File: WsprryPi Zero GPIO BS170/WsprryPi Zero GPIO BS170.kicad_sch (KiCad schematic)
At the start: 28 parts, among them J11 Socket_2x20_P2.54mm, J12 Conn_01x03, J41 SMA_Adafruit_1865, J42 J81/J82 LPF sockets, SW11 SKRPANE010, T21 WBC2-1TLC, T41 WBC2-1TLC, U11 Raspberry Pi 40-pin HAT inter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, U31 LTC6432AIUF-15#PBF, U51 TPS22918DBVR

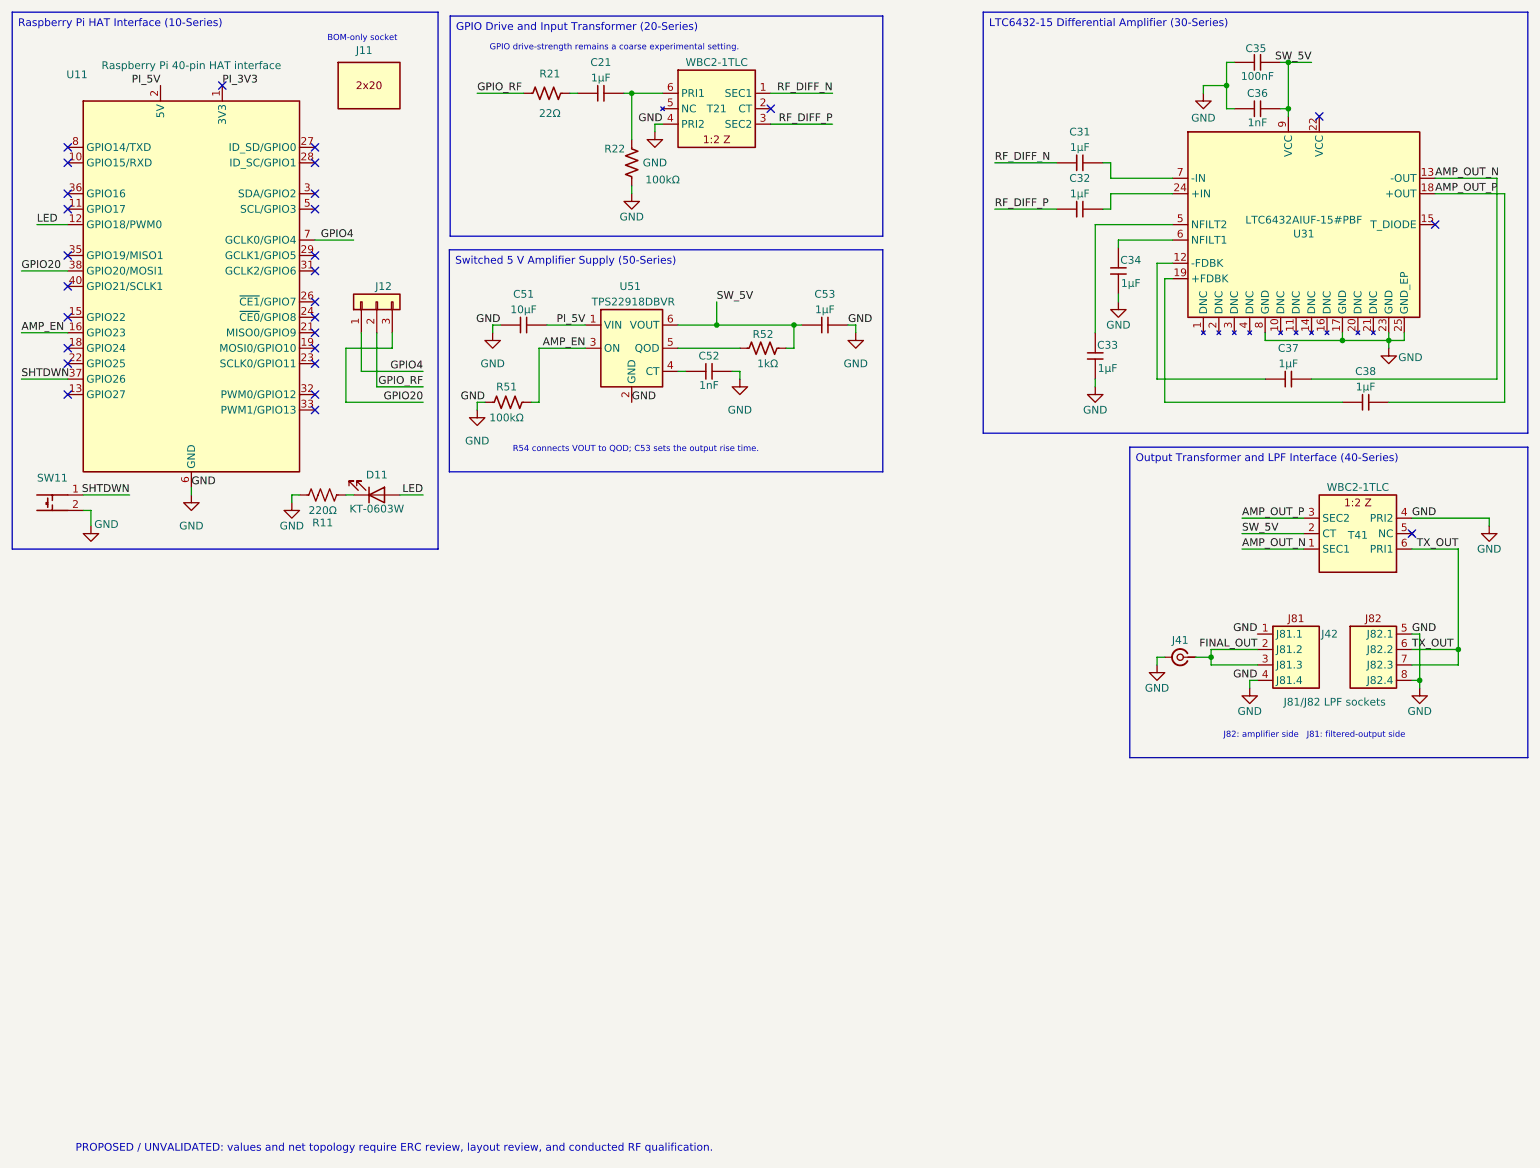
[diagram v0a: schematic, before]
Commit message: Universal GPIO wBS170
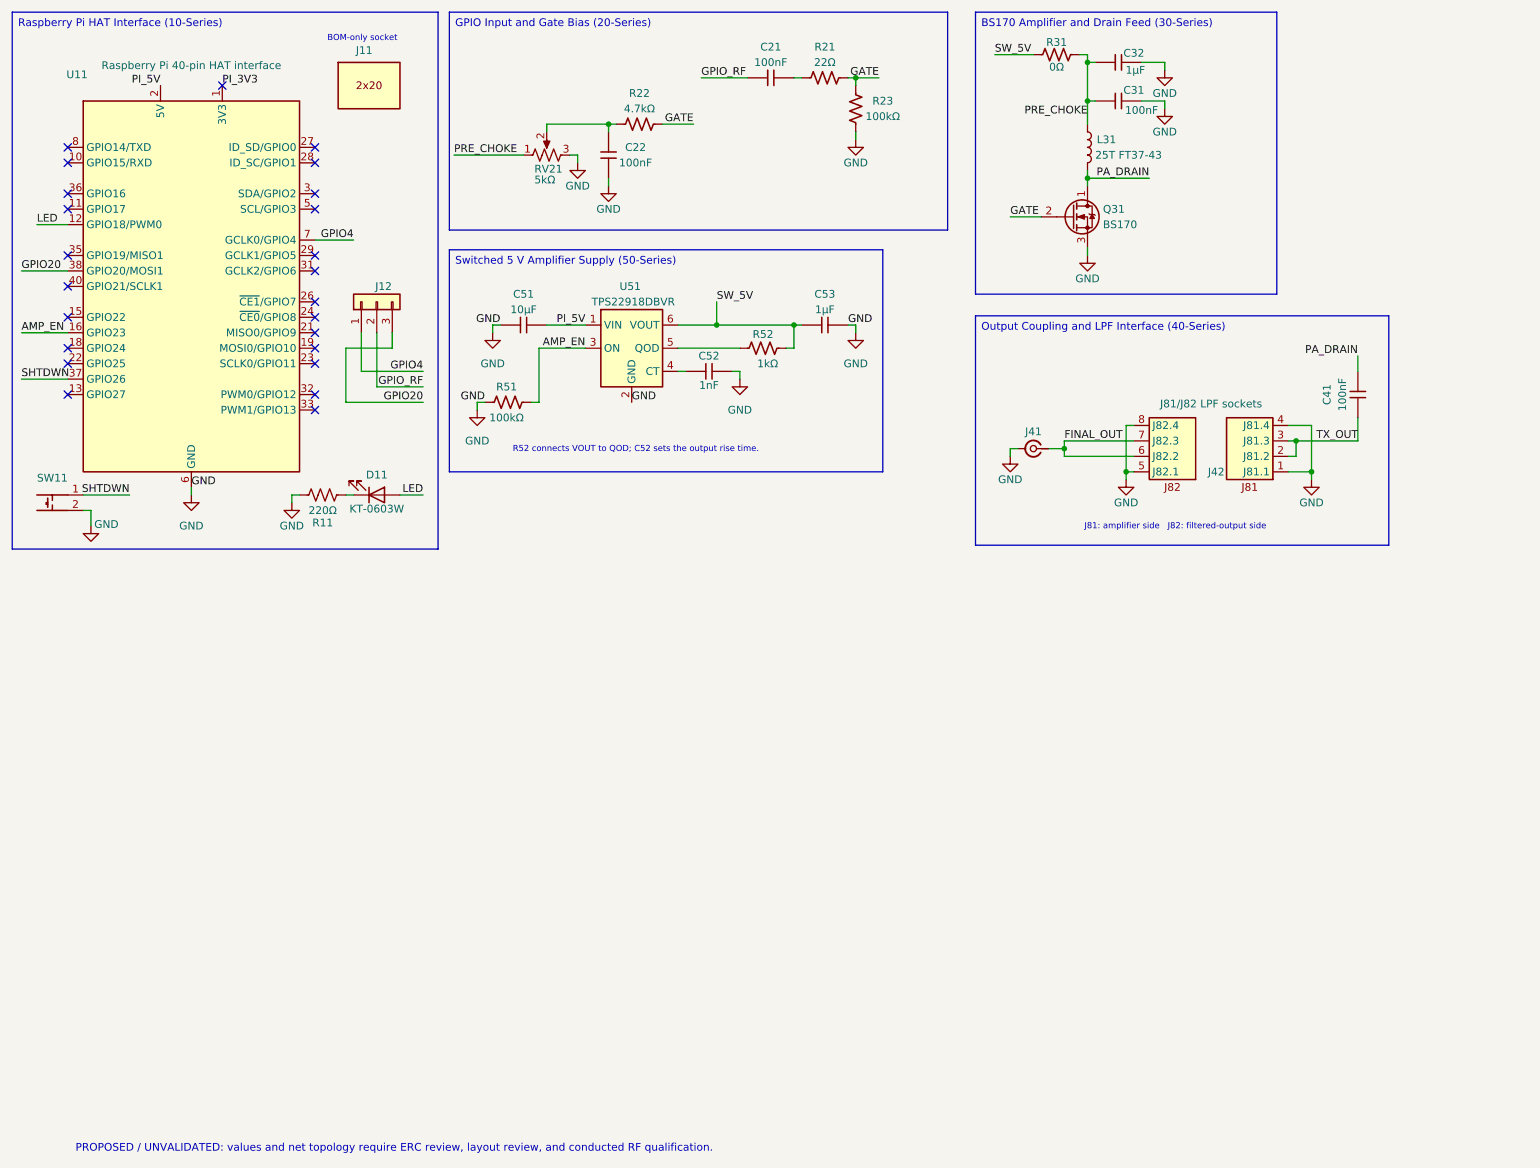
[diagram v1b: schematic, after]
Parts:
- removed C21, C31, C37, C38: 1µF, wsprrypi-zero-gpio-bs170:C_1206_3216Metric, symbol wsprrypi-zero-gpio-bs170:C_0805
- removed C33, C34: 1µF, wsprrypi-zero-gpio-bs170:C_0805_2012Metric, symbol wsprrypi-zero-gpio-bs170:C_0805
- removed C35: 100nF, wsprrypi-zero-gpio-bs170:C_0603_1608Metric, symbol wsprrypi-zero-gpio-bs170:C_0603
- removed C36: 1nF, wsprrypi-zero-gpio-bs170:C_0603_1608Metric, symbol wsprrypi-zero-gpio-bs170:C_0603
- removed T21, T41: WBC2-1TLC, wsprrypi-zero-gpio-bs170:Coilcraft_WBC2-1TLC, symbol wsprrypi-zero-gpio-bs170:WBC2-1TLC
- removed U31: LTC6432AIUF-15#PBF, wsprrypi-zero-gpio-bs170:Analog_UF24_QFN-24-1EP_4x4mm_P0.5mm_EP2.45x2.45mm_ThermalVias, symbol wsprrypi-zero-gpio-bs170:LTC6432-15
- added C21, C22, C31, C41: 100nF, wsprrypi-zero-gpio-bs170:C_0603_1608Metric, symbol wsprrypi-zero-gpio-bs170:C_0603
- added L31: 25T FT37-43, wsprrypi-zero-gpio-bs170:L_Toroid_FT37-43_Vertical_P5.08mm, symbol wsprrypi-zero-gpio-bs170:L
- added Q31: BS170, wsprrypi-zero-gpio-bs170:TO-92_Inline, symbol wsprrypi-zero-gpio-bs170:BS170
- added R23: 100kΩ, wsprrypi-zero-gpio-bs170:R_0603_1608Metric, symbol wsprrypi-zero-gpio-bs170:R_0603
- added R31: 0Ω, wsprrypi-zero-gpio-bs170:R_0805_2012Metric, symbol wsprrypi-zero-gpio-bs170:R_0805
- added RV21: 5kΩ, wsprrypi-zero-gpio-bs170:Potentiometer_Bourns_TC33X_Vertical, symbol wsprrypi-zero-gpio-bs170:R_Potentiometer_US
- C32: footprint wsprrypi-zero-gpio-bs170:C_1206_3216Metric -> wsprrypi-zero-gpio-bs170:C_0805_2012Metric; LCSC_PART C342628 -> (none)
- J42: now left out of the parts list
- R21: LCSC_PART C23186 -> (none)
- R22: value 100kΩ -> 4.7kΩ; LCSC_PART C14675 -> (none)
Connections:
- net RF_DIFF_P is gone; now on net GND: C32.1
- net FINAL_OUT: now also J42.6 (J82.2), J42.7 (J82.3); no longer J42.2 (J81.2), J42.3 (J81.3)
- net GND: now also C22.1, C31.1, Q31.3 (S), R23.1, RV21.3; no longer R22.1
- net GPIO_RF: now also C21.1; no longer R21.1
- net SW_5V: now also R31.1
- net TX_OUT: now also J42.2 (J81.2), J42.3 (J81.3), C41.1; no longer J42.6 (J82.2), J42.7 (J82.3)
- net PRE_CHOKE: now reaches C32.2
- net PRE_CHOKE: now also C31.2, L31.1, R31.2, RV21.1
- net GATE: now reaches R22.2
- net GATE: now also R21.2, Q31.2 (G), R23.2
- new net: C21.2, R21.1
- new net: C22.2, R22.1, RV21.2
- new net PA_DRAIN: C41.2, L31.2, Q31.1 (D)
- no-connect marks 28 -> 24
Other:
- note added: "J81: amplifier side J82: filtered-output side"
- note added: "R52 connects VOUT to QOD; C52 sets the output rise time."
- note removed: "GPIO drive-strength remains a coarse experimental setting."
- note removed: "J82: amplifier side J81: filtered-output side"
- note removed: "R54 connects VOUT to QOD; C53 sets the output rise time."
- title: WsprryPi Zero GPIO BS170 - Copied LTC6432 Baseline -> WsprryPi Zero GPIO BS170 - Unwired RF Stage
- moved on the sheet: J41, J42

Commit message: Renumber BS170 functional blocks and component references
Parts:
- renumbered C51 to C21, C52 to C22, C53 to C23, C21 to C31, C22 to C32, C31 to C41, C32 to C42, C41 to C51, J41 to J51, J42 to J52, L31 to L41, Q31 to Q41, R51 to R21, R52 to R22, R21 to R31, R22 to R32, R23 to R33, R31 to R41, RV21 to RV31, U51 to U21
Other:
- note added: "R22 connects VOUT to QOD; C22 sets the output rise time."
- note removed: "R52 connects VOUT to QOD; C52 sets the output rise time."
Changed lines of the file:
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@@
 		)
 	)
-	(text "R52 connects VOUT to QOD; C52 sets the output rise time."
+	(text "R22 connects VOUT to QOD; C22 sets the output rise time."
 		(exclude_from_sim no)
 		(at 97.282 87.122 0)
@@
 		)
 	)
-	(text_box "Output Coupling and LPF Interface (40-Series)"
+	(text_box "Output Coupling and LPF Interface (50-Series)"
 		(exclude_from_sim no)
 		(at 173.355 64.53 0)
@@
 		)
 	)
-	(text_box "GPIO Input and Gate Bias (20-Series)"
+	(text_box "GPIO Input and Gate Bias (30-Series)"
 		(exclude_from_sim no)
 		(at 86.86 14.605 0)
@@
 		)
 	)
-	(text_box "Switched 5 V Amplifier Supply (50-Series)"
+	(text_box "Switched 5 V Amplifier Supply (20-Series)"
 		(exclude_from_sim no)
 		(at 86.86 53.67 0)
@@
 		)
 	)
-	(text_box "BS170 Amplifier and Drain Feed (30-Series)"
+	(text_box "BS170 Amplifier and Drain Feed (40-Series)"
 		(exclude_from_sim no)
 		(at 173.355 14.605 0)
@@
 		(in_pos_files yes)
 		(dnp no)
-		(property "Reference" "C31"
+		(property "Reference" "C41"
 			(at 199.39 27.432 0)
 			(show_name no)
@@
 			(project "WsprryPi Zero GPIO BS170"
 				(path "/42fb2efa-c288-4686-a90a-043ad23a327d"
-					(reference "C31")
+					(reference "C41")
 					(unit 1)
 				)
@@
 		(in_pos_files yes)
 		(dnp no)
-		(property "Reference" "R21"
+		(property "Reference" "R31"
 			(at 148.59 20.32 0)
 			(show_name no)
@@
 			(project "WsprryPi Zero GPIO BS170"
 				(path "/42fb2efa-c288-4686-a90a-043ad23a327d"
-					(reference "R21")
+					(reference "R31")
 					(unit 1)
 				)
@@
 		(in_pos_files yes)
 		(dnp no)
-		(property "Reference" "C22"
+		(property "Reference" "C32"
 			(at 117.475 36.83 90)
 			(show_name no)
@@
 			(project "WsprryPi Zero GPIO BS170"
 				(path "/42fb2efa-c288-4686-a90a-043ad23a327d"
-					(reference "C22")
+					(reference "C32")
 					(unit 1)
 				)
@@
 		(in_pos_files yes)
 		(dnp no)
-		(property "Reference" "C21"
+		(property "Reference" "C31"
 			(at 139.7 20.32 0)
 			(show_name no)
@@
 			(project "WsprryPi Zero GPIO BS170"
 				(path "/42fb2efa-c288-4686-a90a-043ad23a327d"
-					(reference "C21")
+					(reference "C31")
 					(unit 1)
 				)
@@
 		(in_pos_files yes)
 		(dnp no)
-		(property "Reference" "J41"
+		(property "Reference" "J51"
 			(at 182.88 83.566 0)
 			(show_name no)
@@
 			(project "WsprryPi Zero GPIO BS170"
 				(path "/42fb2efa-c288-4686-a90a-043ad23a327d"
-					(reference "J41")
+					(reference "J51")
 					(unit 1)
 				)
@@
 		(in_pos_files no)
 		(dnp no)
-		(property "Reference" "L31"
+		(property "Reference" "L41"
 			(at 193.294 35.56 0)
 			(show_name no)
@@
 			(project "WsprryPi Zero GPIO BS170"
 				(path "/42fb2efa-c288-4686-a90a-043ad23a327d"
-					(reference "L31")
+					(reference "L41")
 					(unit 1)
 				)
@@
 		(in_pos_files yes)
 		(dnp no)
-		(property "Reference" "R23"
+		(property "Reference" "R33"
 			(at 158.115 29.21 90)
 			(show_name no)
@@
 			(project "WsprryPi Zero GPIO BS170"
 				(path "/42fb2efa-c288-4686-a90a-043ad23a327d"
-					(reference "R23")
+					(reference "R33")
 					(unit 1)
 				)
@@
 		(in_pos_files yes)
 		(dnp no)
-		(property "Reference" "C53"
+		(property "Reference" "C23"
 			(at 148.59 60.96 0)
 			(show_name no)
@@
 			(project "WsprryPi Zero GPIO BS170"
 				(path "/42fb2efa-c288-4686-a90a-043ad23a327d"
-					(reference "C53")
+					(reference "C23")
 					(unit 1)
 				)
@@
 		(in_pos_files yes)
 		(dnp no)
-		(property "Reference" "C32"
+		(property "Reference" "C42"
 			(at 199.39 21.336 0)
 			(show_name no)
@@
 			(project "WsprryPi Zero GPIO BS170"
 				(path "/42fb2efa-c288-4686-a90a-043ad23a327d"
-					(reference "C32")
+					(reference "C42")
 					(unit 1)
 				)
@@
 		(in_pos_files yes)
 		(dnp no)
-		(property "Reference" "C51"
+		(property "Reference" "C21"
 			(at 99.06 60.96 0)
 			(show_name no)
@@
 			(project "WsprryPi Zero GPIO BS170"
 				(path "/42fb2efa-c288-4686-a90a-043ad23a327d"
-					(reference "C51")
+					(reference "C21")
 					(unit 1)
 				)
@@
 		(in_pos_files yes)
 		(dnp no)
-		(property "Reference" "R22"
+		(property "Reference" "R32"
 			(at 118.11 27.94 0)
 			(show_name no)
@@
 			(project "WsprryPi Zero GPIO BS170"
 				(path "/42fb2efa-c288-4686-a90a-043ad23a327d"
-					(reference "R22")
+					(reference "R32")
 					(unit 1)
 				)
@@
 		(in_pos_files yes)
 		(dnp no)
-		(property "Reference" "Q31"
+		(property "Reference" "Q41"
 			(at 194.31 46.99 0)
 			(show_name no)
@@
 			(project "WsprryPi Zero GPIO BS170"
 				(path "/42fb2efa-c288-4686-a90a-043ad23a327d"
-					(reference "Q31")
+					(reference "Q41")
 					(unit 1)
 				)
@@
 		(in_pos_files no)
 		(dnp no)
-		(property "Reference" "J42"
+		(property "Reference" "J52"
 			(at 212.93 90.18 0)
 			(show_name no)
@@
 			(project "WsprryPi Zero GPIO BS170"
 				(path "/42fb2efa-c288-4686-a90a-043ad23a327d"
-					(reference "J42")
+					(reference "J52")
 					(unit 1)
 				)
@@
 		(in_pos_files yes)
 		(dnp no)
-		(property "Reference" "R31"
+		(property "Reference" "R41"
 			(at 186.69 19.558 0)
 			(show_name no)
@@
 			(project "WsprryPi Zero GPIO BS170"
 				(path "/42fb2efa-c288-4686-a90a-043ad23a327d"
-					(reference "R31")
+					(reference "R41")
 					(unit 1)
 				)
@@
 		(in_pos_files yes)
 		(dnp no)
-		(property "Reference" "C52"
+		(property "Reference" "C22"
 			(at 129.54 71.12 0)
 			(show_name no)
@@
 			(project "WsprryPi Zero GPIO BS170"
 				(path "/42fb2efa-c288-4686-a90a-043ad23a327d"
-					(reference "C52")
+					(reference "C22")
 					(unit 1)
 				)
@@
 		(in_pos_files yes)
 		(dnp no)
-		(property "Reference" "U51"
+		(property "Reference" "U21"
 			(at 116.586 59.69 0)
 			(show_name no)
@@
 			(project "WsprryPi Zero GPIO BS170"
 				(path "/42fb2efa-c288-4686-a90a-043ad23a327d"
-					(reference "U51")
+					(reference "U21")
 					(unit 1)
 				)
@@
 		(in_pos_files yes)
 		(dnp no)
-		(property "Reference" "RV21"
+		(property "Reference" "RV31"
 			(at 100.838 40.386 90)
 			(show_name no)
@@
 			(project "WsprryPi Zero GPIO BS170"
 				(path "/42fb2efa-c288-4686-a90a-043ad23a327d"
-					(reference "RV21")
+					(reference "RV31")
 					(unit 1)
 				)
@@
 		(in_pos_files yes)
 		(dnp no)
-		(property "Reference" "R51"
+		(property "Reference" "R21"
 			(at 96.266 76.2 0)
 			(show_name no)
@@
 			(project "WsprryPi Zero GPIO BS170"
 				(path "/42fb2efa-c288-4686-a90a-043ad23a327d"
-					(reference "R51")
+					(reference "R21")
 					(unit 1)
 				)
@@
 		(in_pos_files yes)
 		(dnp no)
-		(property "Reference" "C41"
+		(property "Reference" "C51"
 			(at 231.14 77.47 0)
 			(show_name no)
@@
 			(project "WsprryPi Zero GPIO BS170"
 				(path "/42fb2efa-c288-4686-a90a-043ad23a327d"
-					(reference "C41")
+					(reference "C51")
 					(unit 1)
 				)
@@
 		(in_pos_files yes)
 		(dnp no)
-		(property "Reference" "R52"
+		(property "Reference" "R22"
 			(at 138.43 67.564 0)
 			(show_name no)
@@
 			(project "WsprryPi Zero GPIO BS170"
 				(path "/42fb2efa-c288-4686-a90a-043ad23a327d"
-					(reference "R52")
+					(reference "R22")
 					(unit 1)
 				)

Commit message: File rename and cleanup
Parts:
- J52: value J81/J82 LPF sockets -> LPF female headers; footprint wsprrypi-zero-gpio-bs170:Dual_PinSocket_1x04_P2.54mm_J81_J82 -> wsprrypi-zero-gpio-bs170:LPF_HeaderPair_Female_2x1x04_P2.54mm_S33.02mm; symbol wsprrypi-zero-gpio-bs170:Dual_PinSocket_1x04_P2.54mm_J81_J82 -> wsprrypi-zero-gpio-bs170:LPF_HeaderPair_Female_2x1x04_P2.54mm_S33.02mm
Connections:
- net FINAL_OUT: now also C51.2, J52.2 (RF_IN), J52.3 (RF_IN); no longer J51.1 (In), J52.6 (J82.2), J52.7 (J82.3)
- net PA_DRAIN: now also C51.1; no longer C51.2
- net TX_OUT: now also J51.1 (In), J52.6 (RF_OUT), J52.7 (RF_OUT); no longer C51.1, J52.2 (J81.2), J52.3 (J81.3)
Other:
- note removed: "J81: amplifier side J82: filtered-output side"
- note removed: "R22 connects VOUT to QOD; C22 sets the output rise time."
- moved on the sheet: C21, C22, C23, C31, C32, C41, C42, C51, D11, J11, J12, J51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
